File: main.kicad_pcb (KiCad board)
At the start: 2 copper layers, 228.6 x 70.6 mm, 132 parts, among them J1 Conn_02x16_Row_Letter_First, J2 Conn_01x05, J3 Conn_01x02, J4 Screw_Terminal_01x02, J5 Screw_Terminal_01x10, J6 Screw_Terminal_01x10, J7 Screw_Terminal_01x02, J8 Screw_Terminal_01x10, J9 Screw_Terminal_01x10, U1 TPS73233DBVR, U10 TLP3558A, U11 TLP3558A, U12 TLP3558A, U13 TLP3558A, U14 TLP3558A, U15 TLP3558A, U16 TLP3558A, U17 TLP3558A, U18 TLP3558A, U19 TLP3558A, U20 TLP3558A, U21 TLP3558A, U22 TLP3558A, U23 TLP3558A, U24 TLP3558A, U25 TLP3558A, U26 TLP3558A, U27 TLP3558A, U28 TLP3558A, U29 TLP3558A, U3 STM32G070KBT6, U30 TLP3558A, U31 TLP3558A, U32 TLP3558A, U33 TLP3558A, U34 TLP3558A, U35 TLP3558A, U36 TLP3558A, U37 TLP3558A, U38 TLP3558A, U39 TLP3558A, U4 TLP3558A, U40 TLP3558A, U41 TLP3558A, U42 TLP3558A, U43 TLP3558A, U44 TLP3558A, U45 TLP3558A, U46 TLP3558A, U47 TLP3558A, U5 TLP3558A, U6 TLP3558A, U7 TLP3558A, U8 TLP3558A, U9 TLP3558A

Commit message: Kicad 7 lib updates and track cleanup
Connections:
- net +3V3 renamed +3.3V

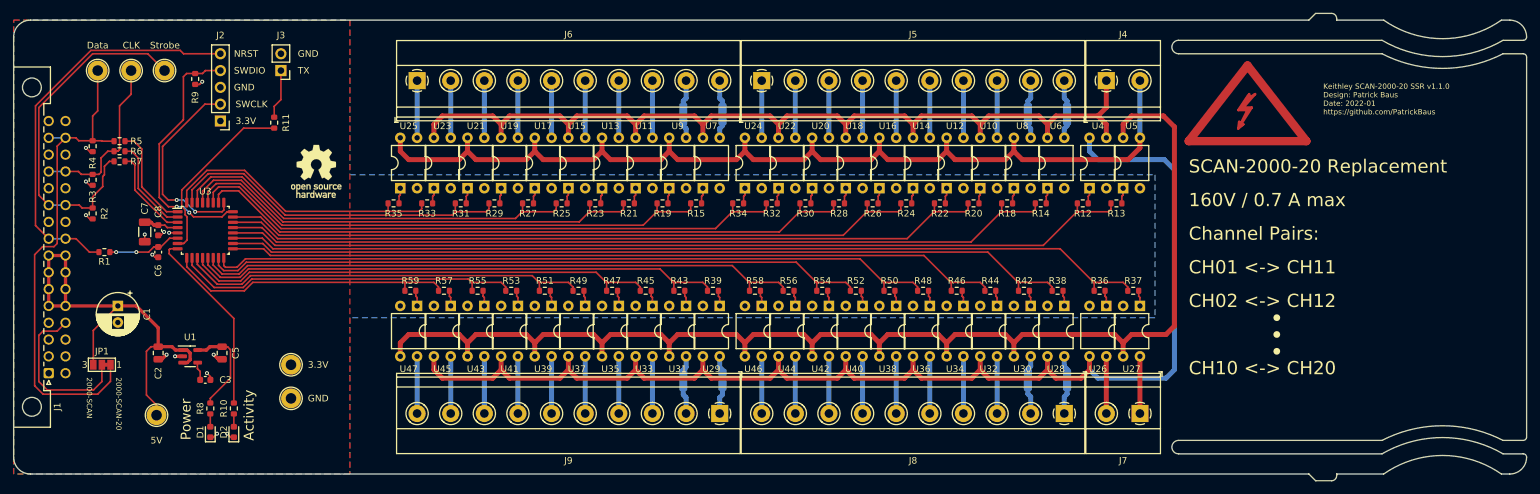
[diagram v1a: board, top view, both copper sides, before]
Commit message: added flatcable connector, updated doc
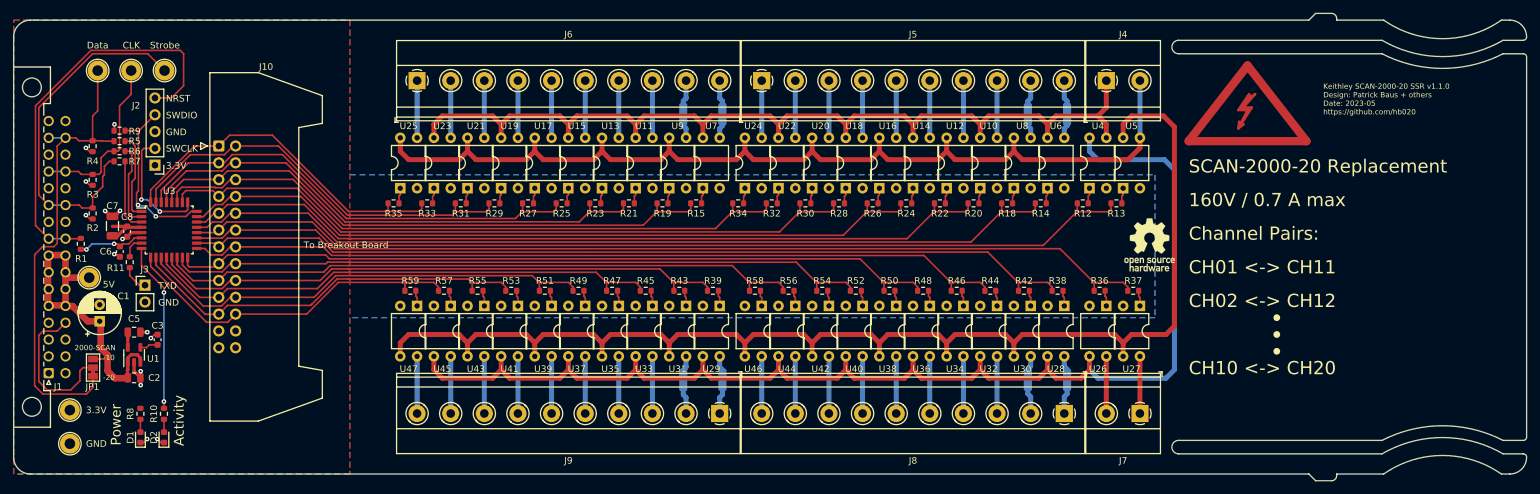
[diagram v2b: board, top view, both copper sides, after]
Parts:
- added J10: Conn_01x26_Pin, Connector_IDC:IDC-Header_2x13_P2.54mm_Latch_Horizontal, F.Cu at (56.4, 67.3)
- moved LOGO2 126.4 mm to (197.0, 82.2)
- moved J3 38.4 mm to (45.2, 88.3), turned to 0 degrees
- moved TP2 34.1 mm to (33.9, 107.2)
- moved TP3 34.1 mm to (33.9, 112.3)
- moved R11 30.3 mm to (43.0, 84.8), turned to 90 degrees
- moved TP1 23.1 mm to (36.8, 87.2)
- moved R9 13.8 mm to (41.4, 65.0), turned to 180 degrees
- moved C5 13.7 mm to (43.6, 95.4), turned to 0 degrees
- moved J2 11.9 mm to (46.8, 70.2)
- moved D1 10.6 mm to (44.6, 111.3)
- moved D2 10.6 mm to (48.1, 111.3)
- moved R10 10.6 mm to (48.1, 107.7)
- moved R8 10.6 mm to (44.6, 107.7)
- moved C3 9.41 mm to (47.2, 96.6), turned to 90 degrees
- moved U1 8.47 mm to (43.6, 98.8), turned to 90 degrees
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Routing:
- net /Microcontroller/TX: track 27.4 -> 3.38 mm
- net +5V: track 68.8 -> 51.3 mm
- net /Microcontroller/SWCLK: track 30.2 -> 18.5 mm
- net /Microcontroller/SWDIO: track 38.4 -> 26.9 mm
- net +3.3V: track 20.0 -> 9.41 mm
- net /Microcontroller/CH10: track 43.4 -> 53.2 mm
- net /Microcontroller/CH20: track 43.6 -> 53.0 mm
- net /Microcontroller/CH19: track 52.8 -> 61.7 mm
- net /Microcontroller/CH9: track 53.0 -> 61.5 mm
- net /Microcontroller/CH8: track 62.2 -> 70.5 mm
- net /Microcontroller/CH18: track 62.1 -> 70.3 mm
- net /Microcontroller/CH3: track 105.8 -> 114.0 mm
- net /Microcontroller/CH7: track 71.5 -> 79.2 mm
- net /Microcontroller/CH17: track 71.5 -> 79.1 mm
- net /Microcontroller/CH1: track 126.3 -> 133.8 mm
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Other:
- board text added: "-10"
- board text added: "-20"
- board text added: "Keithley SCAN-2000-20 SSR v1.1.0 Design: Patrick Baus + others Date: 2023-05 https://github.com/hb020"
- board text added: "Room above PCB = 15mm"
- board text added: "TXD"
- board text added: "To Breakout Board"
- board text removed: "2000-SCAN-20"
- board text removed: "Keithley SCAN-2000-20 SSR v1.1.0 Design: Patrick Baus Date: 2022-01 https://github.com/PatrickBaus"
- board text removed: "TX"

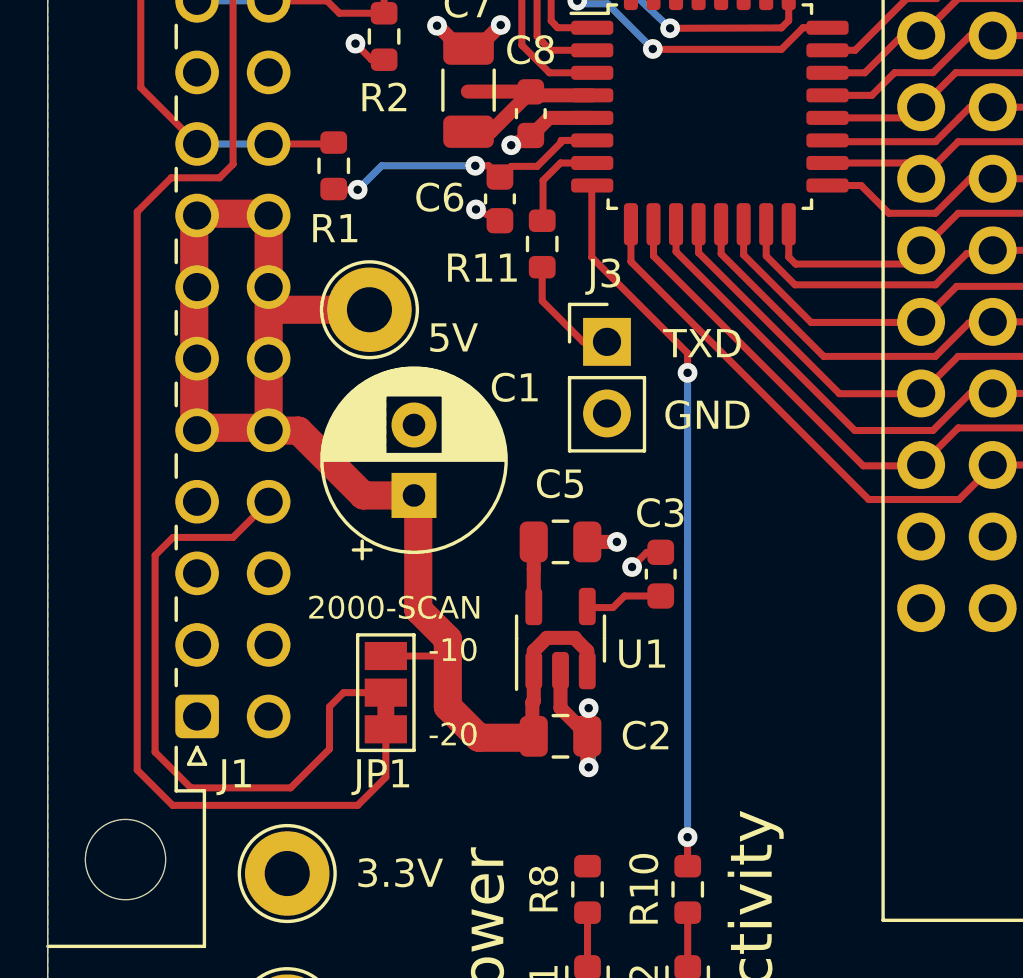
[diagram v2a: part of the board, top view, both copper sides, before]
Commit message: update after component procurement problems
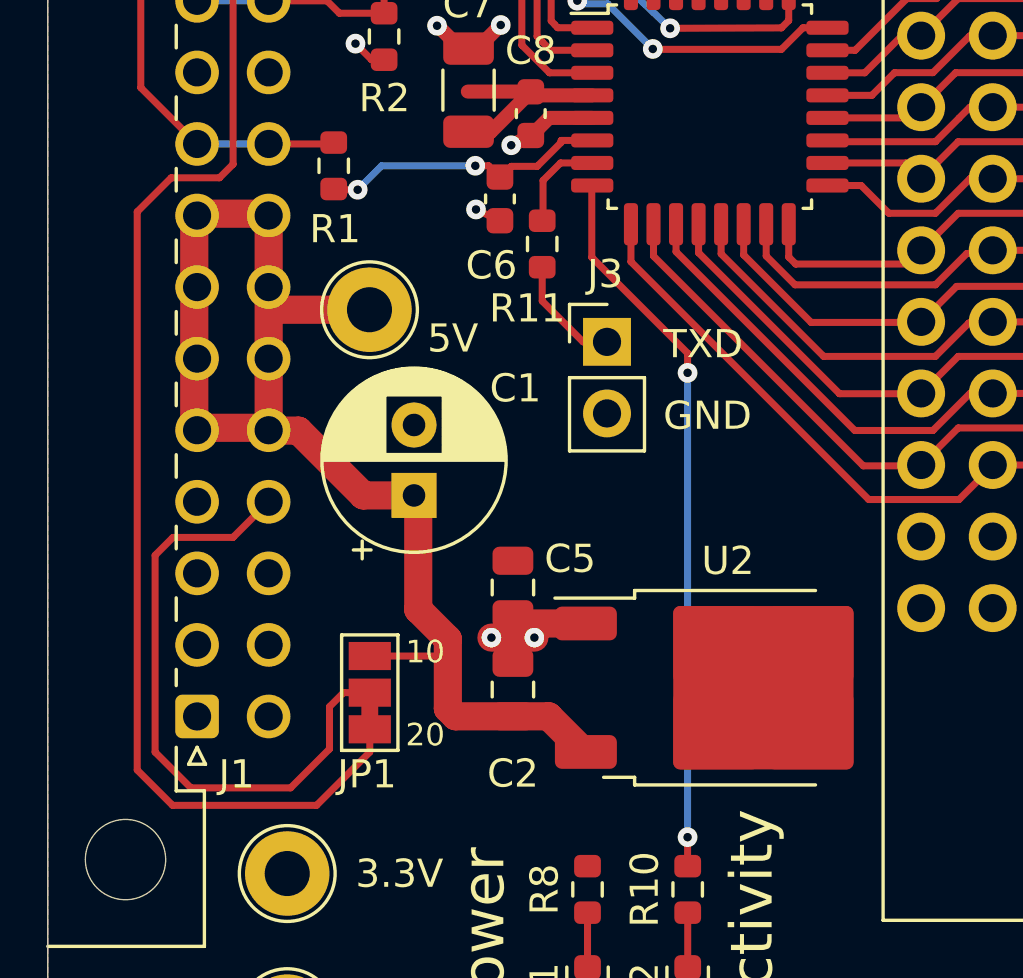
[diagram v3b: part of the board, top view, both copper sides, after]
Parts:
- removed C3: 100n, Capacitor_SMD:C_0603_1608Metric
- removed U1: TPS73233DBVR, Package_TO_SOT_SMD:SOT-23-5
- added U2: NCP1117-3.3_TO252, Package_TO_SOT_SMD:TO-252-2, F.Cu at (49.5, 100.6)
- C2, C5: value 1u -> 10u
- moved C2 2.37 mm to (41.9, 100.7), turned to 90 degrees
- moved C5 2.34 mm to (41.9, 97.0), turned to -90 degrees
- moved JP1 0.57 mm to (36.8, 100.8)
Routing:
- net +5V: track 51.3 -> 45.7 mm
- net GND: track 21.9 -> 18.9 mm, vias 14 -> 12
- net Net-(U1-NR): track 2.78 -> 0.00 mm
- net +3.3V: track 9.41 -> 7.13 mm
- net /DATA: track 72.7 -> 71.7 mm
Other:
- board text added: "10"
- board text added: "20"
- board text removed: "-10"
- board text removed: "-20"
- board text removed: "2000-SCAN"

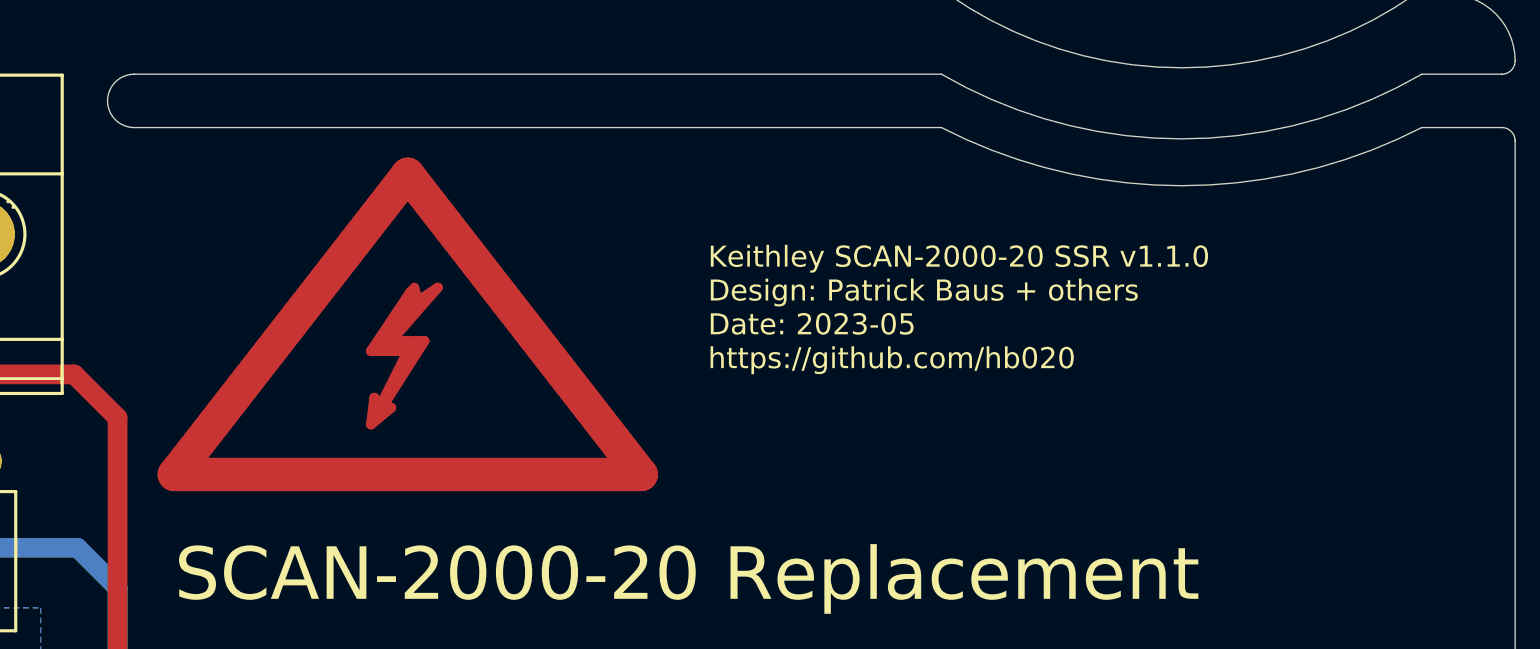
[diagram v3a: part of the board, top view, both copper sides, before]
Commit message: version on silkscreen was wrong
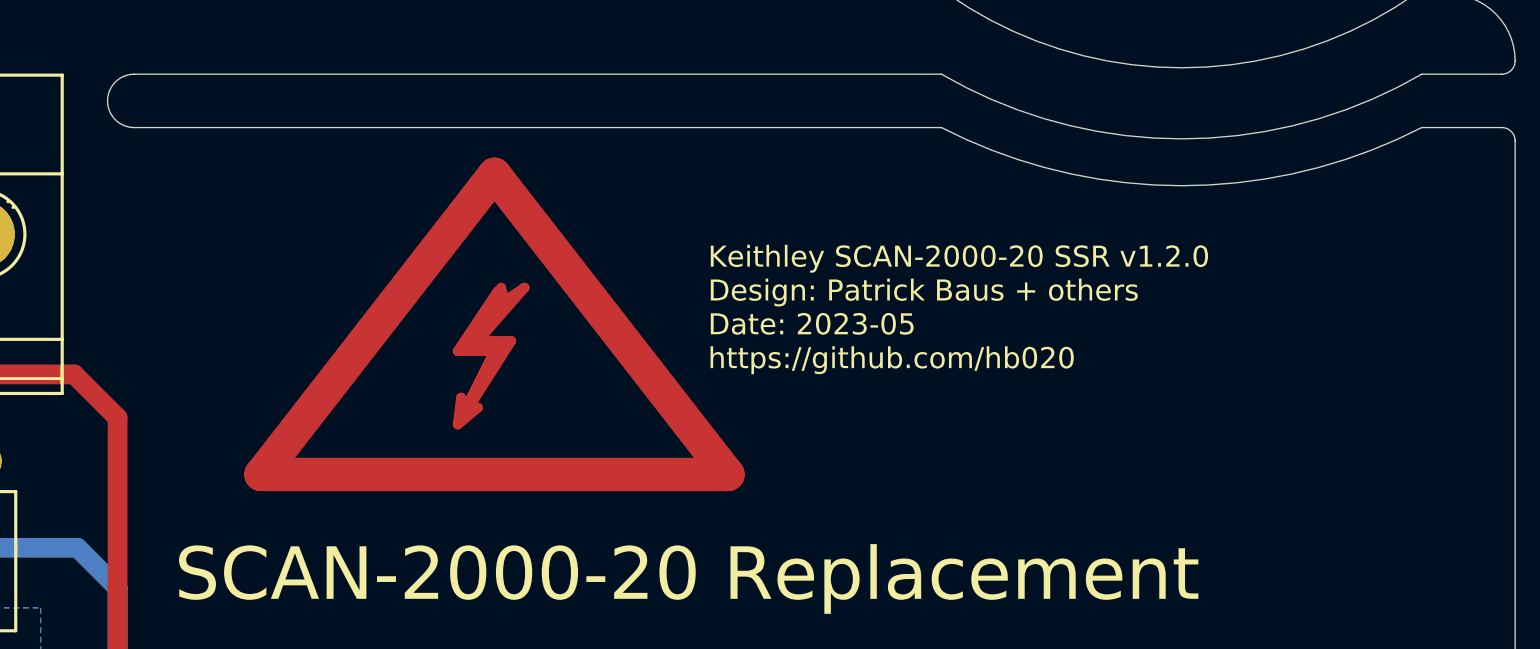
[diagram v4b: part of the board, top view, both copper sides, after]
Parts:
- moved SYM1 3.30 mm to (215.1, 62.7)
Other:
- board text added: "Keithley SCAN-2000-20 SSR v1.2.0 Design: Patrick Baus + others Date: 2023-05 https://github.com/hb020"
- board text added: "Room vertically above PCB = 15mm"
- board text removed: "Keithley SCAN-2000-20 SSR v1.1.0 Design: Patrick Baus + others Date: 2023-05 https://github.com/hb020"
- board text removed: "Room above PCB = 15mm"
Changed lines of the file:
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@@
   (net 131 "Net-(J9-Pin_10)")
   (footprint "Symbol:Symbol_Highvoltage_Type2_CopperTop_Small" (layer "F.Cu")
-    (at 211.836 62.738)
+    (at 215.138 62.738)
     (descr "Symbol, Highvoltage, Type 2, Copper Top, Small,")
     (tags "Symbol, Highvoltage, Type 2, Copper Top, Small,")
@@
   (gr_line (start 221.1166 116.84) (end 222.123 117.856)
     (stroke (width 0.05) (type solid)) (layer "Edge.Cuts"))
-  (gr_text "Keithley SCAN-2000-20 SSR v1.1.0\nDesign: Patrick Baus + others\nDate: 2023-05\nhttps://github.com/hb020" (at 223.266 60.198) (layer "F.SilkS")
+  (gr_text "Keithley SCAN-2000-20 SSR v1.2.0\nDesign: Patrick Baus + others\nDate: 2023-05\nhttps://github.com/hb020" (at 223.266 60.198) (layer "F.SilkS")
     (effects (font (size 0.8 0.8) (thickness 0.15)) (justify left))
   )
@@
     (effects (font (size 1 1) (thickness 0.15)))
   )
-  (gr_text "Room above PCB = 15mm" (at 259.08 59.69) (layer "Dwgs.User")
+  (gr_text "Room vertically above PCB = 15mm" (at 259.08 59.69) (layer "Dwgs.User")
     (effects (font (size 1 1) (thickness 0.15)) (justify left bottom))
   )

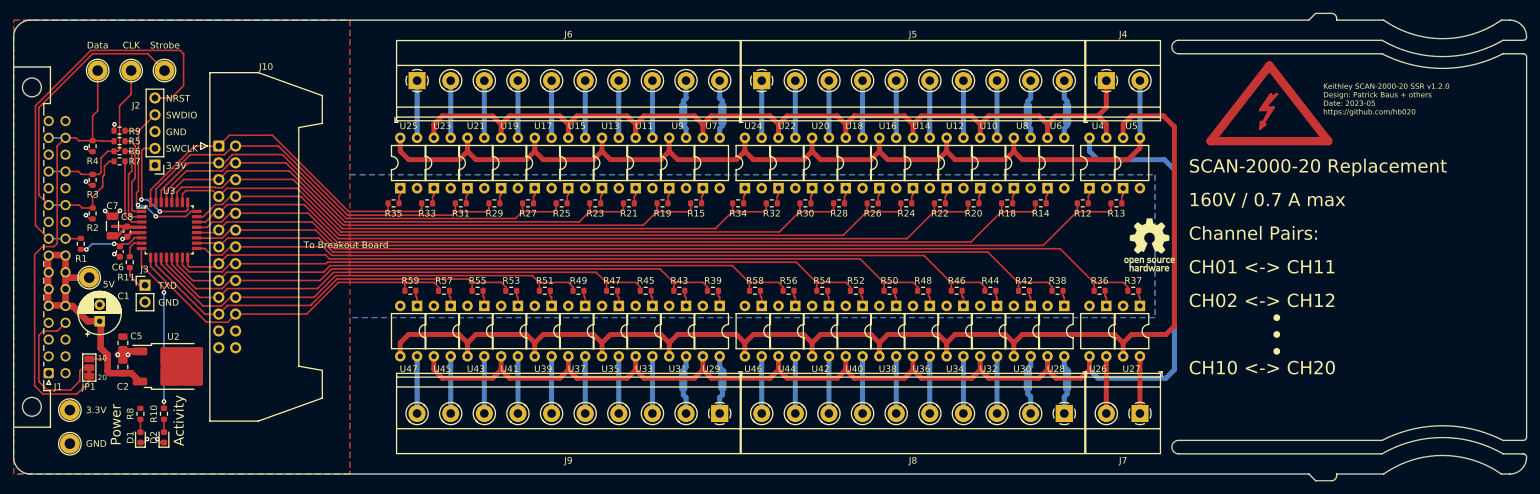
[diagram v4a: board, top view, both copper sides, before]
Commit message: added ARM10-SWD connector
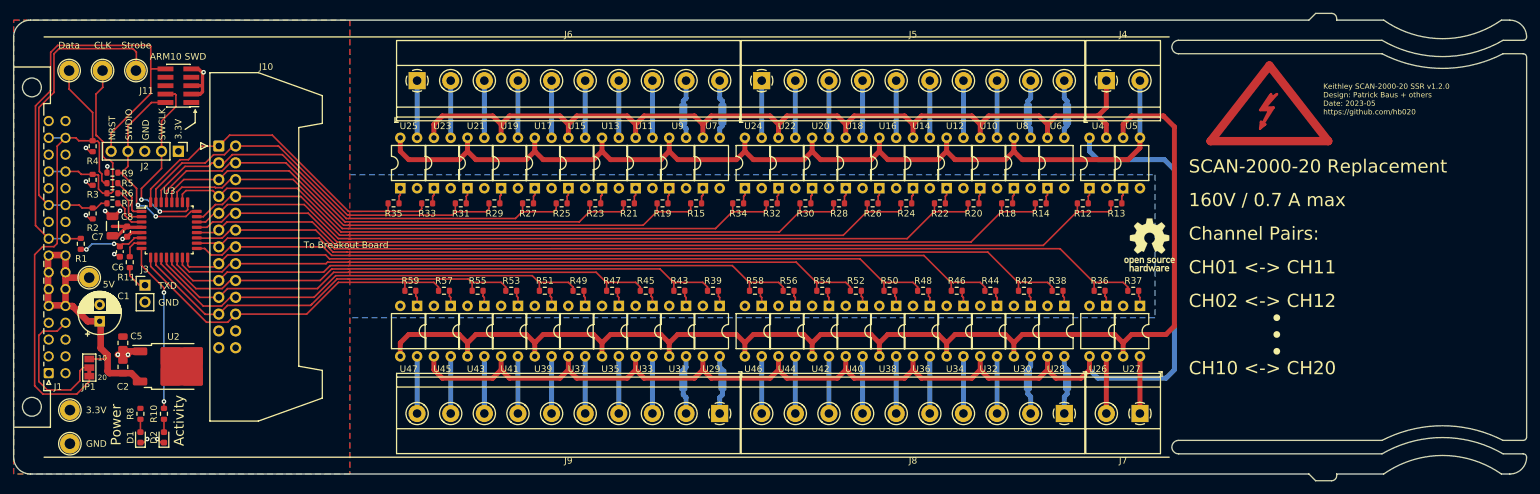
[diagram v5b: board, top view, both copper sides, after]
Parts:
- added J11: Conn_ARM_JTAG_SWD_10, Connector_PinHeader_1.27mm:PinHeader_2x05_P1.27mm_Vertical_SMD, F.Cu at (50.3, 58.2)
- moved R9 6.44 mm to (40.3, 71.3)
- moved R5 6.44 mm to (40.3, 72.9)
- moved R6 6.44 mm to (40.3, 74.4)
- moved R7 6.44 mm to (40.3, 75.9)
- moved TP4 4.32 mm to (33.8, 55.9)
- moved TP6 4.32 mm to (43.9, 55.9)
- moved TP5 4.32 mm to (38.8, 55.9)
- moved J2 4.12 mm to (50.3, 68.1), turned to -90 degrees
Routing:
- net /Microcontroller/SWCLK: track 18.5 -> 28.6 mm
- net /~{NRST}: track 61.8 -> 70.2 mm
- net GND: track 18.9 -> 26.2 mm, vias 12 -> 13
- net /Microcontroller/DATA: track 13.2 -> 6.44 mm
- net /Microcontroller/CLK: track 12.6 -> 6.17 mm
- net /CLK: track 26.4 -> 32.4 mm
- net /Microcontroller/STROBE: track 11.1 -> 5.06 mm
- net /DATA: track 71.7 -> 77.3 mm
- net /Microcontroller/SWDIO: track 26.9 -> 31.8 mm
- net /STROBE: track 54.4 -> 49.6 mm
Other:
- board text added: "ARM10 SWD"
